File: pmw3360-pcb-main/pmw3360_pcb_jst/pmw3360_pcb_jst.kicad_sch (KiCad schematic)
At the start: 21 parts, among them J1 JST_BM08B-GHS-TBT, U1 IC_PMW3360DM-T2QU, U2 LDO_TLV74318PDBVR

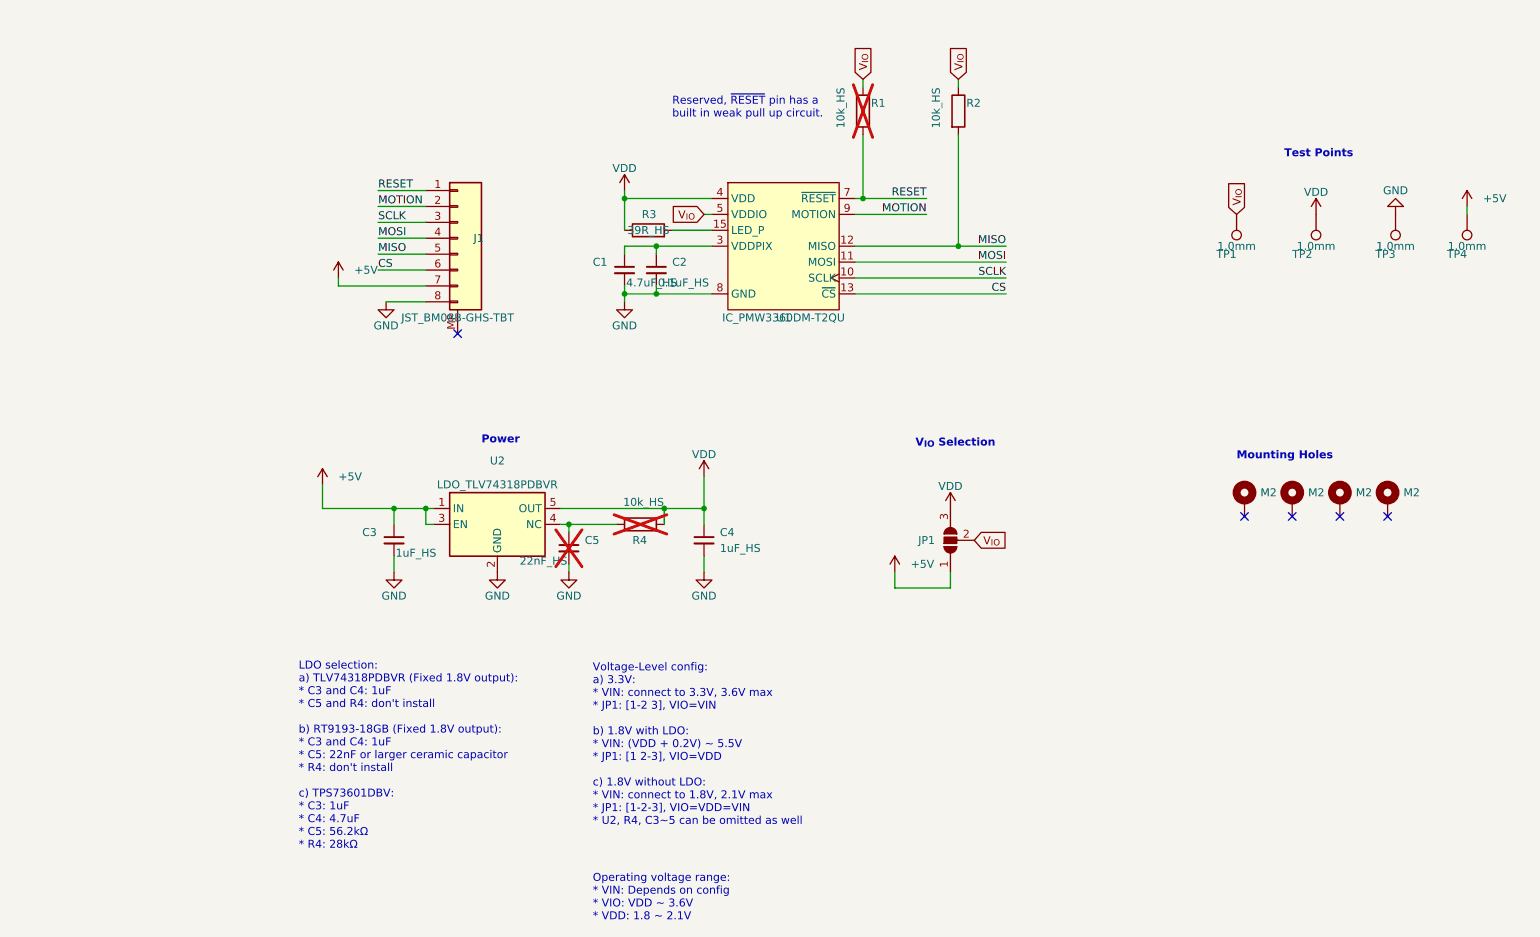
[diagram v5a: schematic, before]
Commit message: wip faceplate 2.0 schematic
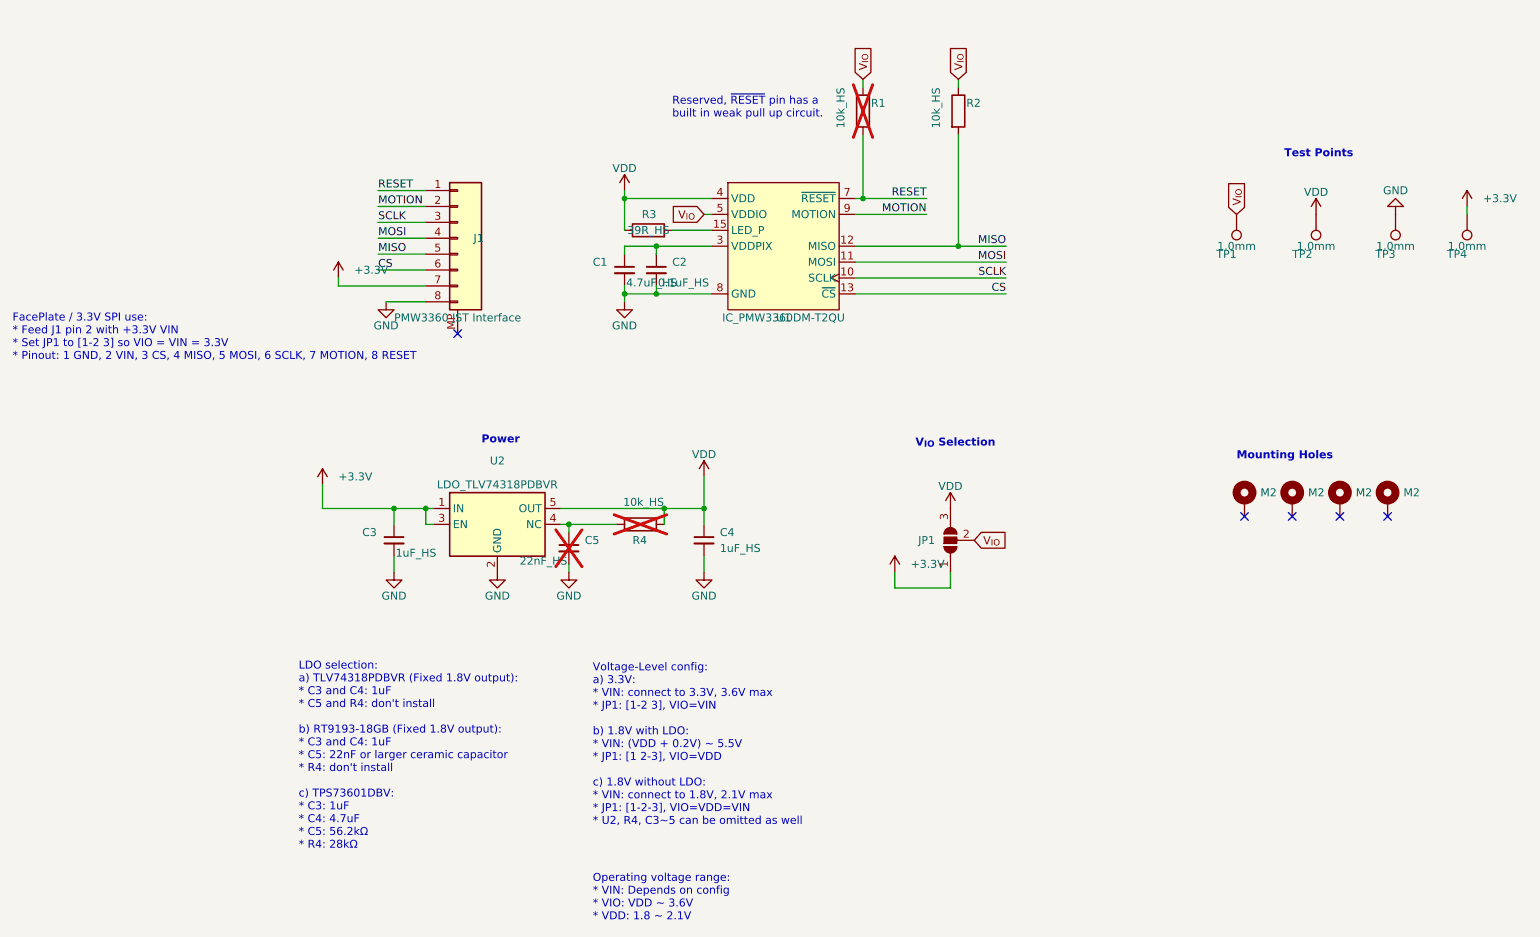
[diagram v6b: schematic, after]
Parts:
- J1: value JST_BM08B-GHS-TBT -> PMW3360 JST Interface
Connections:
- net +5V renamed +3.3V
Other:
- note added: "FacePlate / 3.3V SPI use: * Feed J1 pin 2 with +3.3V VIN * Set JP1 to [1-2 3] so VIO = VIN = 3.3V * Pinout: 1 GND, 2 VIN, 3 CS, 4 MISO, 5 MOSI, 6 SCLK, 7 MOTION, 8 RESET"
